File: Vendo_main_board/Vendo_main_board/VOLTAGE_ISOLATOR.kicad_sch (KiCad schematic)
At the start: 5 parts, among them U1 B0505S-2WR3

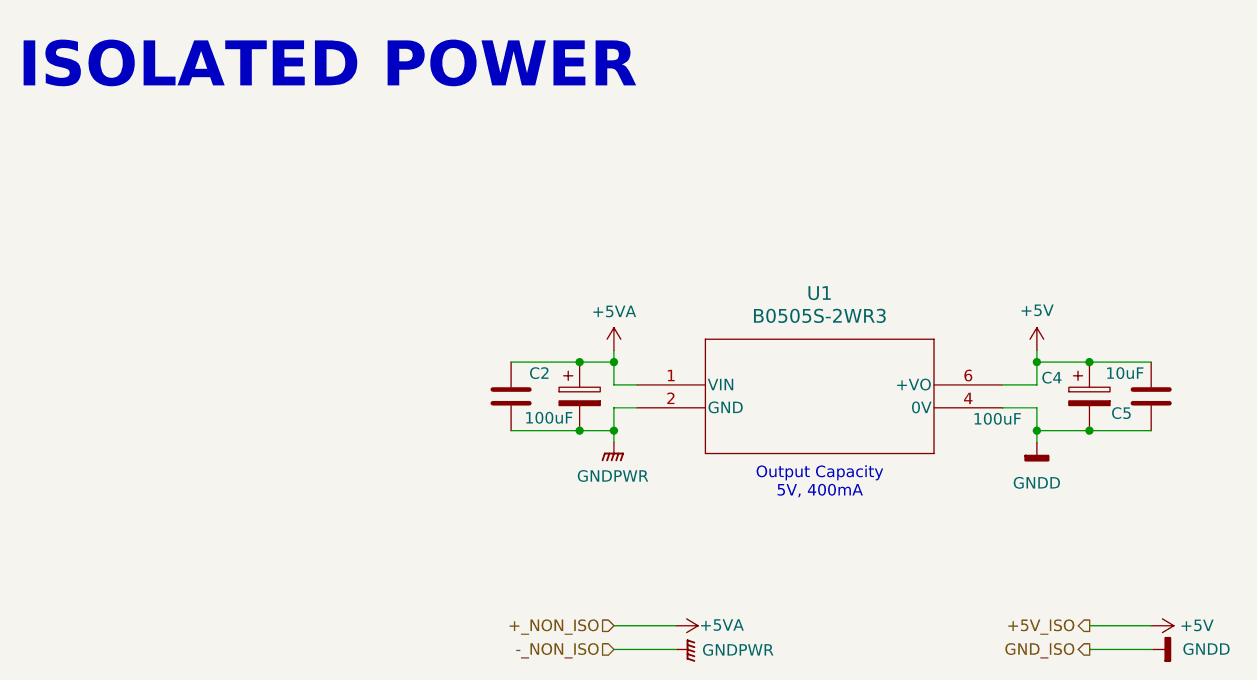
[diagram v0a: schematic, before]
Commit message: -update scheme and pcb placement
update scheme and footprint
added spade connectors
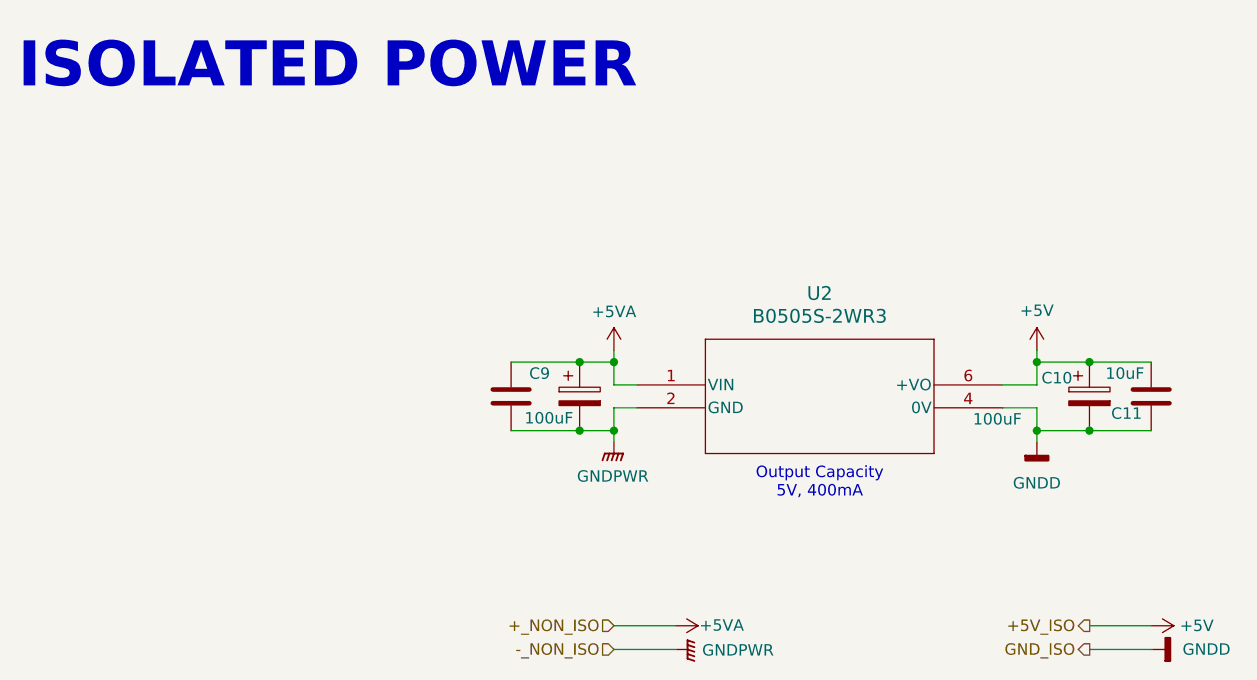
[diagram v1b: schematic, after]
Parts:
- renumbered C4 to C10, C5 to C11, C1 to C8, C2 to C9, U1 to U2
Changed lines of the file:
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@@
 		(on_board yes)
 		(dnp no)
-		(property "Reference" "#PWR08"
+		(property "Reference" "#PWR016"
 			(at 77.7971 52.317 0)
 			(effects
@@
 			(project "Vendo_main_board"
 				(path "/ce68e045-3b24-4b1f-b4c3-20bce3f1de80/1a00dd87-25a6-456f-88e0-9677adfda096"
-					(reference "#PWR08")
+					(reference "#PWR016")
 					(unit 1)
 				)
@@
 		(on_board yes)
 		(dnp no)
-		(property "Reference" "C2"
+		(property "Reference" "C9"
 			(at 68.3745 51.0498 0)
 			(effects
@@
 			(project "Vendo_main_board"
 				(path "/ce68e045-3b24-4b1f-b4c3-20bce3f1de80/1a00dd87-25a6-456f-88e0-9677adfda096"
-					(reference "C2")
+					(reference "C9")
 					(unit 1)
 				)
@@
 		(dnp no)
 		(fields_autoplaced yes)
-		(property "Reference" "#PWR015"
+		(property "Reference" "#PWR021"
 			(at 124.7871 65.017 0)
 			(effects
@@
 			(project "Vendo_main_board"
 				(path "/ce68e045-3b24-4b1f-b4c3-20bce3f1de80/1a00dd87-25a6-456f-88e0-9677adfda096"
-					(reference "#PWR015")
+					(reference "#PWR021")
 					(unit 1)
 				)
@@
 		(on_board yes)
 		(dnp no)
-		(property "Reference" "#PWR0109"
+		(property "Reference" "#PWR018"
 			(at 80.7987 79.0724 0)
 			(effects
@@
 			(project "Vendo_main_board"
 				(path "/ce68e045-3b24-4b1f-b4c3-20bce3f1de80/1a00dd87-25a6-456f-88e0-9677adfda096"
-					(reference "#PWR0109")
+					(reference "#PWR018")
 					(unit 1)
 				)
@@
 		(on_board yes)
 		(dnp no)
-		(property "Reference" "C1"
+		(property "Reference" "C8"
 			(at 65.229 56.2727 0)
 			(effects
@@
 			(project "Vendo_main_board"
 				(path "/ce68e045-3b24-4b1f-b4c3-20bce3f1de80/1a00dd87-25a6-456f-88e0-9677adfda096"
-					(reference "C1")
+					(reference "C8")
 					(unit 1)
 				)
@@
 		(dnp no)
 		(fields_autoplaced yes)
-		(property "Reference" "#PWR09"
+		(property "Reference" "#PWR017"
 			(at 77.7971 63.747 0)
 			(effects
@@
 			(project "Vendo_main_board"
 				(path "/ce68e045-3b24-4b1f-b4c3-20bce3f1de80/1a00dd87-25a6-456f-88e0-9677adfda096"
-					(reference "#PWR09")
+					(reference "#PWR017")
 					(unit 1)
 				)
@@
 		(dnp no)
 		(fields_autoplaced yes)
-		(property "Reference" "U1"
+		(property "Reference" "U2"
 			(at 100.6571 42.157 0)
 			(effects
@@
 			(project "Vendo_main_board"
 				(path "/ce68e045-3b24-4b1f-b4c3-20bce3f1de80/1a00dd87-25a6-456f-88e0-9677adfda096"
-					(reference "U1")
+					(reference "U2")
 					(unit 1)
 				)
@@
 		(on_board yes)
 		(dnp no)
-		(property "Reference" "C5"
+		(property "Reference" "C11"
 			(at 133.0421 55.492 0)
 			(effects
@@
 			(project "Vendo_main_board"
 				(path "/ce68e045-3b24-4b1f-b4c3-20bce3f1de80/1a00dd87-25a6-456f-88e0-9677adfda096"
-					(reference "C5")
+					(reference "C11")
 					(unit 1)
 				)
@@
 		(on_board yes)
 		(dnp no)
-		(property "Reference" "C4"
+		(property "Reference" "C10"
 			(at 125.2951 51.555 0)
 			(effects
@@
 			(project "Vendo_main_board"
 				(path "/ce68e045-3b24-4b1f-b4c3-20bce3f1de80/1a00dd87-25a6-456f-88e0-9677adfda096"
-					(reference "C4")
+					(reference "C10")
 					(unit 1)
 				)
@@
 		(on_board yes)
 		(dnp no)
-		(property "Reference" "#PWR0110"
+		(property "Reference" "#PWR019"
 			(at 89.7832 81.7083 0)
 			(effects
@@
 			(project "Vendo_main_board"
 				(path "/ce68e045-3b24-4b1f-b4c3-20bce3f1de80/1a00dd87-25a6-456f-88e0-9677adfda096"
-					(reference "#PWR0110")
+					(reference "#PWR019")
 					(unit 1)
 				)
@@
 		(dnp no)
 		(fields_autoplaced yes)
-		(property "Reference" "#PWR0111"
+		(property "Reference" "#PWR023"
 			(at 143.9111 81.7083 0)
 			(effects
@@
 			(project "Vendo_main_board"
 				(path "/ce68e045-3b24-4b1f-b4c3-20bce3f1de80/1a00dd87-25a6-456f-88e0-9677adfda096"
-					(reference "#PWR0111")
+					(reference "#PWR023")
 					(unit 1)
 				)
@@
 		(dnp no)
 		(fields_autoplaced yes)
-		(property "Reference" "#PWR014"
+		(property "Reference" "#PWR020"
 			(at 124.7871 52.317 0)
 			(effects
@@
 			(project "Vendo_main_board"
 				(path "/ce68e045-3b24-4b1f-b4c3-20bce3f1de80/1a00dd87-25a6-456f-88e0-9677adfda096"
-					(reference "#PWR014")
+					(reference "#PWR020")
 					(unit 1)
 				)
@@
 		(dnp no)
 		(fields_autoplaced yes)
-		(property "Reference" "#PWR0113"
+		(property "Reference" "#PWR022"
 			(at 133.6566 79.0724 0)
 			(effects
@@
 			(project "Vendo_main_board"
 				(path "/ce68e045-3b24-4b1f-b4c3-20bce3f1de80/1a00dd87-25a6-456f-88e0-9677adfda096"
-					(reference "#PWR0113")
-					(unit 1)
-				)
+					(reference "#PWR022")
+					(unit 1)
+				)
